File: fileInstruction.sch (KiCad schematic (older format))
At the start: 18 parts, among them U10 74AHC1G04, U11 CD74AC238, U12 74AHC1G04, U13 CD74AC238, U14 74AHC08, U15 CD74AC238, U16 74AHC08, U7 74AHCT273, U8 74HC163, U9 CD74AC238

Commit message: Renaming files, cleaning, CHANGELOG
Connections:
- net labels added: BCFG_SPI_CLK, I_BCFG_SPI_CLK, I_OPCHOOSE_CLK, OPCHOOSE_CLK
- net labels removed: BCSPI_CLK, I_BCSPI_CLK, I_OPC_CLK, OPC_CLK
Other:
- note added: "COUNTER :\n0 = Sync bit\n1 = Instruction set with next address\n2 = Simple instruction execution with END,\n Complex instruction execution with next address\n3 = Waiting\n4 = RAM Write with END or END\n"
- note added: "Instruction 5bit :\n0x00 = BWRITE1_CLK\n0x01 = BWRITE2_CLK\n0x02 = BPCS_CLK\n0x03 = OPLEFT_CLK\n0x04 = OPRIGHT_CLK\n0x05 = OPCHOOSE_CLK\n0x06 = PERIPHERAL_CLK\n0x07 = BJMPSRC1_CLK\n0x08 = BJMPSRC2_CLK\n0x09 = BJMPSRC3_CLK\n0x0A = JMPSRC_CLK\n0x0B = BRAMADD1_CLK\n0x0C = BRAMADD2_CLK\n0x0D = SPI_CLK\n0x0E = BCFG_SPI_CLK\n0x0F = STICK\n0x10 = IF\n0x11 = IFNOT\n0x12 = RAMW\n0x13 = UOP\n0x14 = UOP\n0x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"
- note removed: "COUNTER :\n0 = Sync bit\n1 = Instruction set with next\n2 = Instruction clock with END / IF_PULSE_1 / RAM_PULSE_1\n3 = Waiting\n4 = RAM_PULSE_2 with END / END / NEXT\n"
- note removed: "Instruction 5bit :\n0x00 = BWRITE1_CLK\n0x01 = BWRITE2_CLK\n0x02 = BPCS_CLK\n0x03 = OPLEFT_CLK\n0x04 = OPRIGHT_CLK\n0x05 = OPC_CLK\n0x06 = PERIPHERAL_CLK\n0x07 = BJMPSRC1_CLK\n0x08 = BJMPSRC2_CLK\n0x09 = BJMPSRC3_CLK\n0x0A = JMPSRC_CLK\n0x0B = BRAMADD1_CLK\n0x0C = BRAMADD2_CLK\n0x0D = SPI_CLK\n0x0E = BSPI_CLK\n0x0F = STICK\n0x10 = IF\n0x11 = IFNOT\n0x12 = RAMW\n0x13 = UOP\n0x14 = UOP\n0x15 = UOP\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"
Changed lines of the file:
@@
 COUNTER_0
 Text Notes 3850 7350 0    60   ~ 0
-COUNTER :\n0 = Sync bit\n1 = Instruction set with next\n2 = Instruction clock with END / IF_PULSE_1 / RAM_PULSE_1\n3 = Waiting\n4 = RAM_PULSE_2 with END / END / NEXT\n
+COUNTER :\n0 = Sync bit\n1 = Instruction set with next address\n2 = Simple instruction execution with END,\n     Complex instruction execution with next address\n3 = Waiting\n4 = RAM Write with END or END\n
 Text Label 9550 1150 0    60   ~ 0
 I_IF
@@
 I_OPRIGHT_CLK
 Text Label 6400 1650 2    60   ~ 0
-I_OPC_CLK
+I_OPCHOOSE_CLK
 $Comp
 L power:+5V #PWR029
@@
 OPRIGHT_CLK
 Text HLabel 6450 1650 2    60   Output ~ 0
-OPC_CLK
+OPCHOOSE_CLK
 Text HLabel 6450 1850 2    60   Output ~ 0
 BJMPSRC1_CLK
@@
 RAM_OE_CONTROL
 Text Notes 5950 6550 0    60   ~ 0
-Instruction 5bit :\n0x00 = BWRITE1_CLK\n0x01 = BWRITE2_CLK\n0x02 = BPCS_CLK\n0x03 = OPLEFT_CLK\n0x04 = OPRIGHT_CLK\n0x05 = OPC_CLK\n0x06 = PERIPHERAL_CLK\n0x07 = BJMPSRC1_CLK\n0x08 = BJMPSRC2_CLK\n0x09 = BJMPSRC3_CLK\n0x0A = JMPSRC_CLK\n0x0B = BRAMADD1_CLK\n0x0C = BRAMADD2_CLK\n0x0D = SPI_CLK\n0x0E = BSPI_CLK\n0x0F = STICK\n0x10 = IF\n0x11 = IFNOT\n0x12 = RAMW\n0x13 = UOP\n0x14 = UOP\n0x15 = UOP\n0x16 = UOP\n0x17 = LTICK
+Instruction 5bit :\n0x00 = BWRITE1_CLK\n0x01 = BWRITE2_CLK\n0x02 = BPCS_CLK\n0x03 = OPLEFT_CLK\n0x04 = OPRIGHT_CLK\n0x05 = OPCHOOSE_CLK\n0x06 = PERIPHERAL_CLK\n0x07 = BJMPSRC1_CLK\n0x08 = BJMPSRC2_CLK\n0x09 = BJMPSRC3_CLK\n0x0A = JMPSRC_CLK\n0x0B = BRAMADD1_CLK\n0x0C = BRAMADD2_CLK\n0x0D = SPI_CLK\n0x0E = BCFG_SPI_CLK\n0x0F = STICK\n0x10 = IF\n0x11 = IFNOT\n0x12 = RAMW\n0x13 = UOP\n0x14 = UOP\n0x15 = UOP\n0x16 = UOP\n0x17 = LTICK
 Text Label 4600 1700 2    60   ~ 0
 INSTRUCTION_B1
@@
 	5700 1150 6450 1150
 Text HLabel 6450 3600 2    60   Output ~ 0
-BCSPI_CLK
+BCFG_SPI_CLK
 Text HLabel 6450 3500 2    60   Output ~ 0
 SPI_CLK
-Text Label 6400 3600 2    60   ~ 0
-I_BCSPI_CLK
 Text Label 6400 3500 2    60   ~ 0
 I_SPI_CLK
@@
 Wire Bus Line
 	2650 6700 2650 7500
+Text Label 6400 3600 2    60   ~ 0
+I_BCFG_SPI_CLK
 $EndSCHEMATC

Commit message: Apply MM1 memory standard, and shared power pin symbol fix
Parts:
- removed U10, U12: 74AHC1G04, Package_TO_SOT_SMD:SOT-23-5, symbol 74xGxx:74AHC1G04
- removed U11, U13, U15, U9: CD74AC238, Package_SO:SOIC-16_3.9x9.9mm_P1.27mm, symbol 74xx_IEEE:74HC238
- added U10, U12: 74AHC1G04, Package_TO_SOT_SMD:SOT-23-5, symbol Custom:74AHC1G04
- added U11, U13, U15, U9: CD74AC238, Package_SO:SOIC-16_3.9x9.9mm_P1.27mm, symbol Custom:CD74AC238
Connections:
- wire segments 143 -> 145
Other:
- moved on the sheet: C10, C11, C12, C4, C5, C6, C8, U14, U7, U8

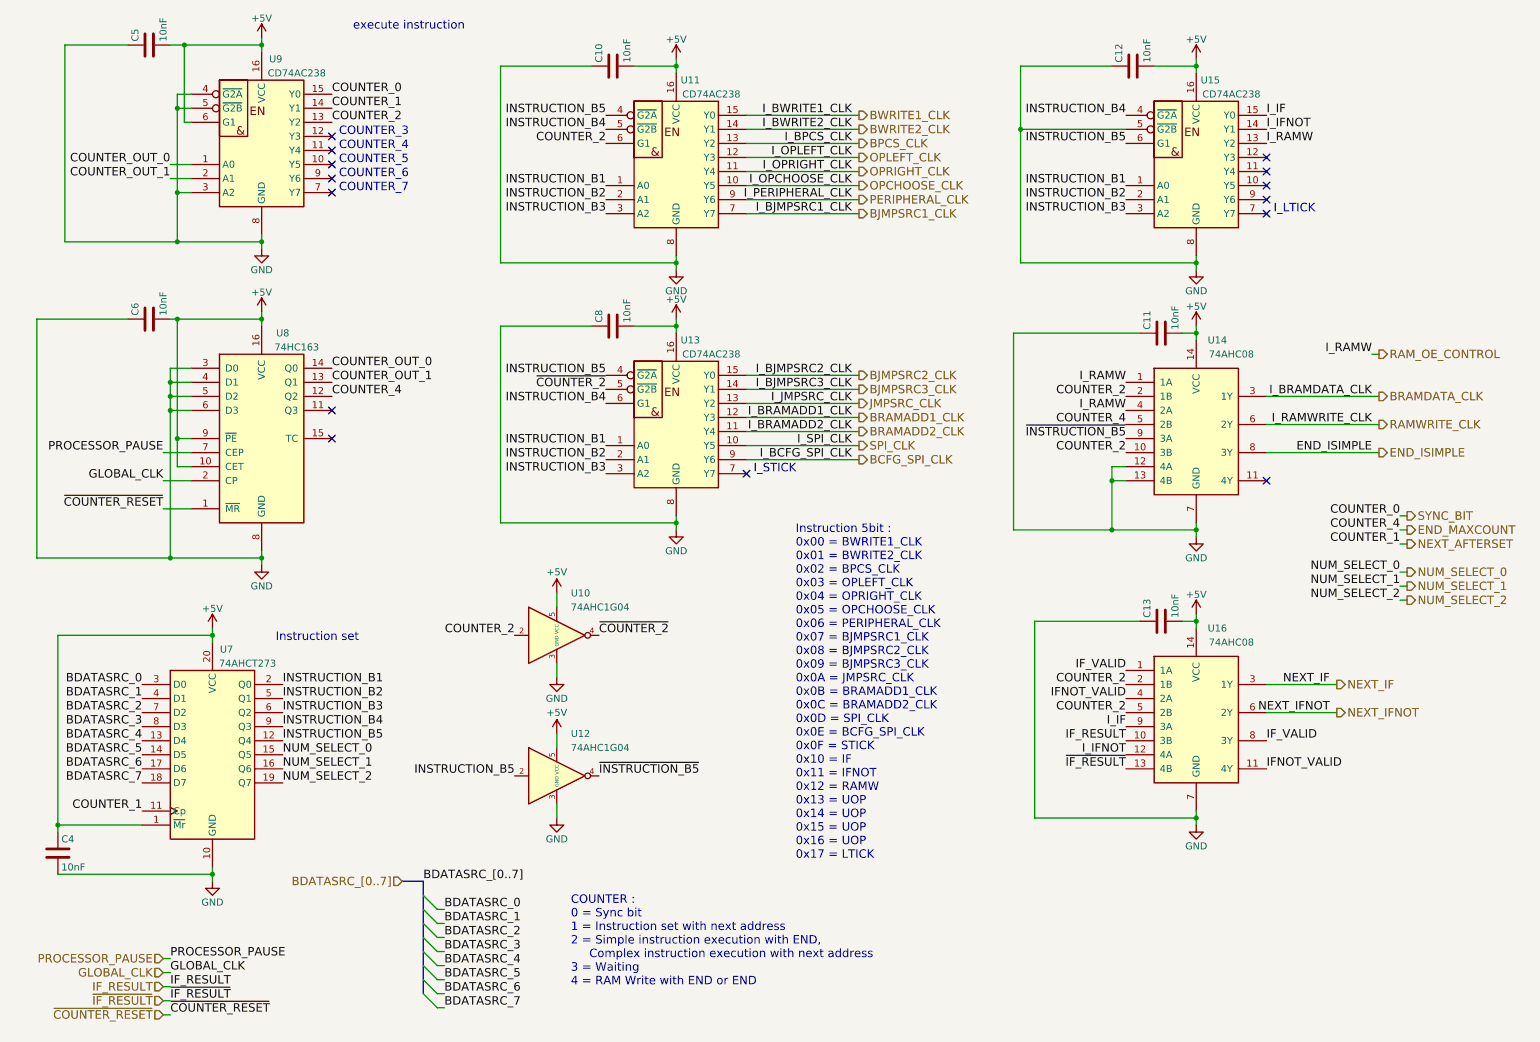
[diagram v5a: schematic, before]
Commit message: V5.1 (#9)
* Apply new symbol for XC2C256-VQ100 #5

* Set new date and 5.1

* Replacing 74HC165 with 74HC166, and add SPI_CFG_DS #4

* Replace some gates with a 74AHC1G02 to fix the pulse problem #3

* Go next only if SRCVALUE, (simple instruction)

* Remove weird ghost bus in register

* Small cleaning in fileRegister

* Go next only if SRCVALUE, (complex instruction) #8
adding 74AHC1G08

* Better decoupling #6

* Component association (#7)

* netlist

* Updated BOM for V5.1

* Routing, cleaning first pass

* bit of pcb cleaning

* SolderMaskClearance to 0

* Schematics to pdf

* PCB files in pdf

* exporting Gerbert files

* new 3d images

* Update README.md

* Modifying CHANGELOG file

* Update README.md
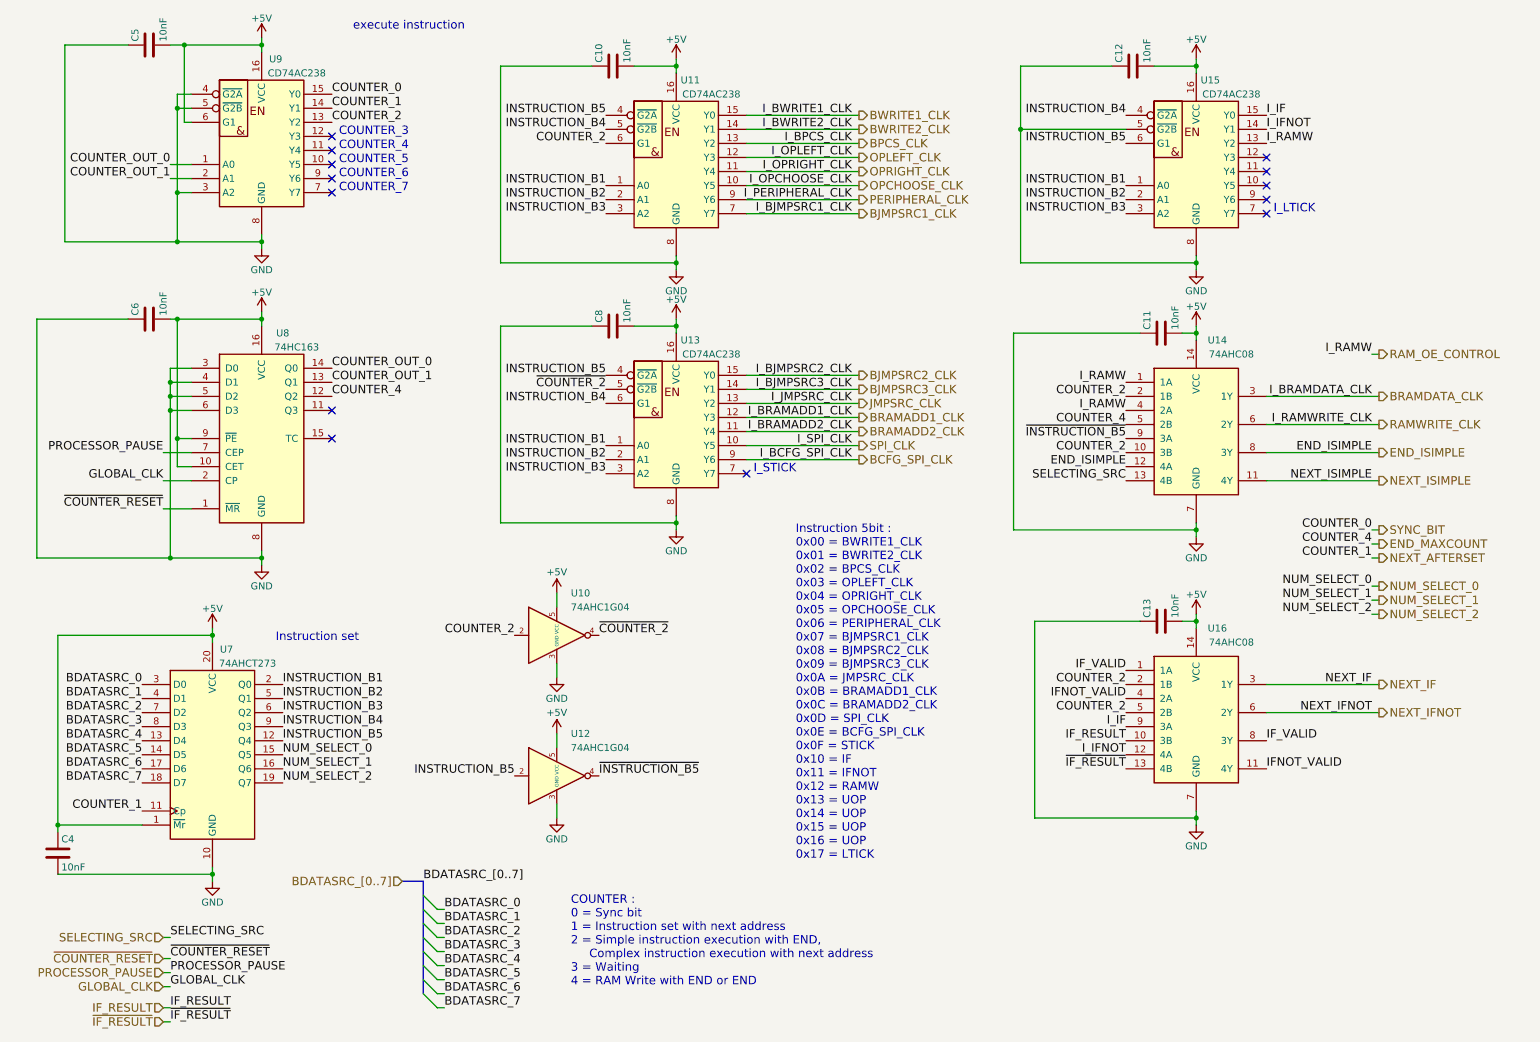
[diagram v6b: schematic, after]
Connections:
- net END_ISIMPLE: now also U14.12 (4A)
- net GND: no longer U14.12 (4A), U14.13 (4B)
- net NEXT_ISIMPLE: now reaches U14.11 (4Y)
- new net SELECTING_SRC: U14.13 (4B)
- no-connect marks 14 -> 13
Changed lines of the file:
@@
 Sheet 6 8
 Title "GP8B"
-Date "2020-08-19"
-Rev "V5.0"
+Date "2021-03-04"
+Rev "V5.1"
 Comp "Guillaume Guillet"
-Comment1 "Copyright Guillaume Guillet 2020"
+Comment1 "Copyright Guillaume Guillet 2021"
 Comment2 "Licensed under CERN-OHL-W v2 or later"
 Comment3 ""
@@
 	1    0    0    -1
 $EndComp
-Text Label 9750 5300 2    60   ~ 0
+Text Label 10050 5300 2    60   ~ 0
 NEXT_IF
 Text Label 6350 1950 2    60   ~ 0
@@
 Text Label 8300 5900 2    60   ~ 0
 ~IF_RESULT
-Text Label 9750 5500 2    60   ~ 0
+Text Label 10050 5500 2    60   ~ 0
 NEXT_IFNOT
 Text Label 9300 5700 0    60   ~ 0
@@
 Text Label 8300 5400 2    60   ~ 0
 IFNOT_VALID
-Text HLabel 1450 7350 0    60   Input ~ 0
+Text HLabel 1450 7450 0    60   Input ~ 0
 GLOBAL_CLK
-Text Label 1500 7350 0    60   ~ 0
+Text Label 1500 7450 0    60   ~ 0
 GLOBAL_CLK
-Text HLabel 1450 7450 0    60   Input ~ 0
+Text HLabel 1450 7600 0    60   Input ~ 0
 IF_RESULT
-Text HLabel 1450 7550 0    60   Input ~ 0
+Text HLabel 1450 7700 0    60   Input ~ 0
 ~IF_RESULT
-Text Label 1500 7450 0    60   ~ 0
+Text Label 1500 7600 0    60   ~ 0
 IF_RESULT
-Text Label 1500 7550 0    60   ~ 0
+Text Label 1500 7700 0    60   ~ 0
 ~IF_RESULT
 Text HLabel 6400 1250 2    60   Output ~ 0
@@
 Text HLabel 6400 1850 2    60   Output ~ 0
 PERIPHERAL_CLK
-Text HLabel 9800 5300 2    60   Output ~ 0
+Text HLabel 10100 5300 2    60   Output ~ 0
 NEXT_IF
-Text HLabel 9800 5500 2    60   Output ~ 0
+Text HLabel 10100 5500 2    60   Output ~ 0
 NEXT_IFNOT
-Text HLabel 10300 4200 2    60   Output ~ 0
-END_MAXCOUNT
-Text HLabel 10300 4300 2    60   Output ~ 0
-NEXT_AFTERSET
-Text Label 10250 4300 2    60   ~ 0
-COUNTER_1
-Text Label 1500 7650 0    60   ~ 0
+Text Label 1500 7250 0    60   ~ 0
 ~COUNTER_RESET
-Text HLabel 1450 7650 0    60   Input ~ 0
+Text HLabel 1450 7250 0    60   Input ~ 0
 ~COUNTER_RESET
-Text Label 10250 4500 2    60   ~ 0
-NUM_SELECT_0
-Text Label 10250 4600 2    60   ~ 0
-NUM_SELECT_1
-Text HLabel 10300 4500 2    60   Output ~ 0
-NUM_SELECT_0
-Text HLabel 10300 4600 2    60   Output ~ 0
-NUM_SELECT_1
 Text Label 9300 1450 0    60   ~ 0
 I_RAMW
@@
 Wire Wire Line
 	9300 3450 10100 3450
-Text HLabel 10300 4100 2    60   Output ~ 0
-SYNC_BIT
-Text Label 10250 4100 2    60   ~ 0
-COUNTER_0
 Text HLabel 3150 6700 0    60   Input ~ 0
 BDATASRC_[0..7]
@@
 Text Label 8300 5500 2    60   ~ 0
 COUNTER_2
-Text Label 10250 4200 2    60   ~ 0
-COUNTER_4
-Text Label 10250 4700 2    60   ~ 0
-NUM_SELECT_2
-Text HLabel 10300 4700 2    60   Output ~ 0
-NUM_SELECT_2
 Text Label 3950 5950 2    60   ~ 0
 INSTRUCTION_B5
@@
 COUNTER_4
 NoConn ~ 2650 1500
-Wire Wire Line
-	8300 3850 8200 3850
-Wire Wire Line
-	8200 3750 8200 3850
-Wire Wire Line
-	8200 3750 8300 3750
-NoConn ~ 9300 3850
 Text Notes 2700 1400 0    60   ~ 0
 COUNTER_3
 NoConn ~ 2650 1400
 Wire Wire Line
-	10300 4200 10250 4200
-Wire Wire Line
-	10250 4300 10300 4300
-Wire Wire Line
-	10250 4100 10300 4100
-Wire Wire Line
-	1500 7350 1450 7350
-Wire Wire Line
 	1500 7450 1450 7450
 Wire Wire Line
-	1450 7550 1500 7550
-Wire Wire Line
-	1500 7650 1450 7650
-Wire Wire Line
-	10250 4500 10300 4500
-Wire Wire Line
-	10250 4600 10300 4600
-Wire Wire Line
-	10250 4700 10300 4700
+	1500 7600 1450 7600
+Wire Wire Line
+	1450 7700 1500 7700
+Wire Wire Line
+	1500 7250 1450 7250
 Wire Wire Line
 	10050 2950 10100 2950
@@
 Wire Wire Line
 	1650 3650 1450 3650
-Text Label 1500 7250 0    60   ~ 0
+Text Label 1500 7350 0    60   ~ 0
 PROCESSOR_PAUSE
-Text HLabel 1450 7250 0    60   Input ~ 0
+Text HLabel 1450 7350 0    60   Input ~ 0
 PROCESSOR_PAUSE
 Wire Wire Line
-	1500 7250 1450 7250
+	1500 7350 1450 7350
 Text Label 3300 6700 0    60   ~ 0
 BDATASRC_[0..7]
@@
 	1    0    0    -1
 $EndComp
-Connection ~ 8200 3850
 Wire Wire Line
 	8800 4150 8800 4200
-Wire Wire Line
-	8800 4200 8200 4200
 Connection ~ 8800 4200
 Wire Wire Line
 	8800 4200 8800 4250
-Wire Wire Line
-	8200 3850 8200 4200
-Connection ~ 8200 4200
-Wire Wire Line
-	8200 4200 7500 4200
 Wire Wire Line
 	8800 2750 8800 2800
@@
 Wire Wire Line
 	8800 6250 8800 6200
-Wire Wire Line
-	9300 5300 9800 5300
-Wire Wire Line
-	9300 5500 9800 5500
 Text Label 6350 3700 2    60   ~ 0
 I_BCFG_SPI_CLK
@@
 	7550 900  7550 1350
 Connection ~ 7550 1350
+Wire Wire Line
+	10050 4800 10100 4800
+Wire Wire Line
+	10050 4700 10100 4700
+Wire Wire Line
+	10050 4600 10100 4600
+Wire Wire Line
+	10050 4200 10100 4200
+Wire Wire Line
+	10050 4400 10100 4400
+Wire Wire Line
+	10100 4300 10050 4300
+Text HLabel 10100 4800 2    60   Output ~ 0
+NUM_SELECT_2
+Text Label 10050 4800 2    60   ~ 0
+NUM_SELECT_2
+Text Label 10050 4300 2    60   ~ 0
+COUNTER_4
+Text Label 10050 4200 2    60   ~ 0
+COUNTER_0
+Text HLabel 10100 4200 2    60   Output ~ 0
+SYNC_BIT
+Text HLabel 10100 4700 2    60   Output ~ 0
+NUM_SELECT_1
+Text HLabel 10100 4600 2    60   Output ~ 0
+NUM_SELECT_0
+Text Label 10050 4700 2    60   ~ 0
+NUM_SELECT_1
+Text Label 10050 4600 2    60   ~ 0
+NUM_SELECT_0
+Text Label 10050 4400 2    60   ~ 0
+COUNTER_1
+Text HLabel 10100 4400 2    60   Output ~ 0
+NEXT_AFTERSET
+Text HLabel 10100 4300 2    60   Output ~ 0
+END_MAXCOUNT
+Text HLabel 1450 7100 0    60   Input ~ 0
+SELECTING_SRC
+Wire Wire Line
+	1500 7100 1450 7100
+Wire Wire Line
+	7500 4200 8800 4200
+Text Label 8300 3750 2    60   ~ 0
+END_ISIMPLE
+Text HLabel 10100 3850 2    60   Output ~ 0
+NEXT_ISIMPLE
+Text Label 10050 3850 2    60   ~ 0
+NEXT_ISIMPLE
+Wire Wire Line
+	9300 3850 10100 3850
+Wire Wire Line
+	9300 5300 10100 5300
+Wire Wire Line
+	9300 5500 10100 5500
+Text Label 1500 7100 0    60   ~ 0
+SELECTING_SRC
+Text Label 8300 3850 2    60   ~ 0
+SELECTING_SRC
 Wire Bus Line
 	3300 6700 3300 7500
